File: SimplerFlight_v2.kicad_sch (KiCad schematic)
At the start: 30 parts, among them J1 USB_B_Micro, J2 Conn_01x04_Pin, J3 Conn_01x04_Pin, J4 Conn_01x04_Pin, J5 Conn_01x04_Pin, J6 675031020, SW1 SW_SPDT, U1 AMS1117-3.3, U2 STM32F401RETx, Y1 16MHz

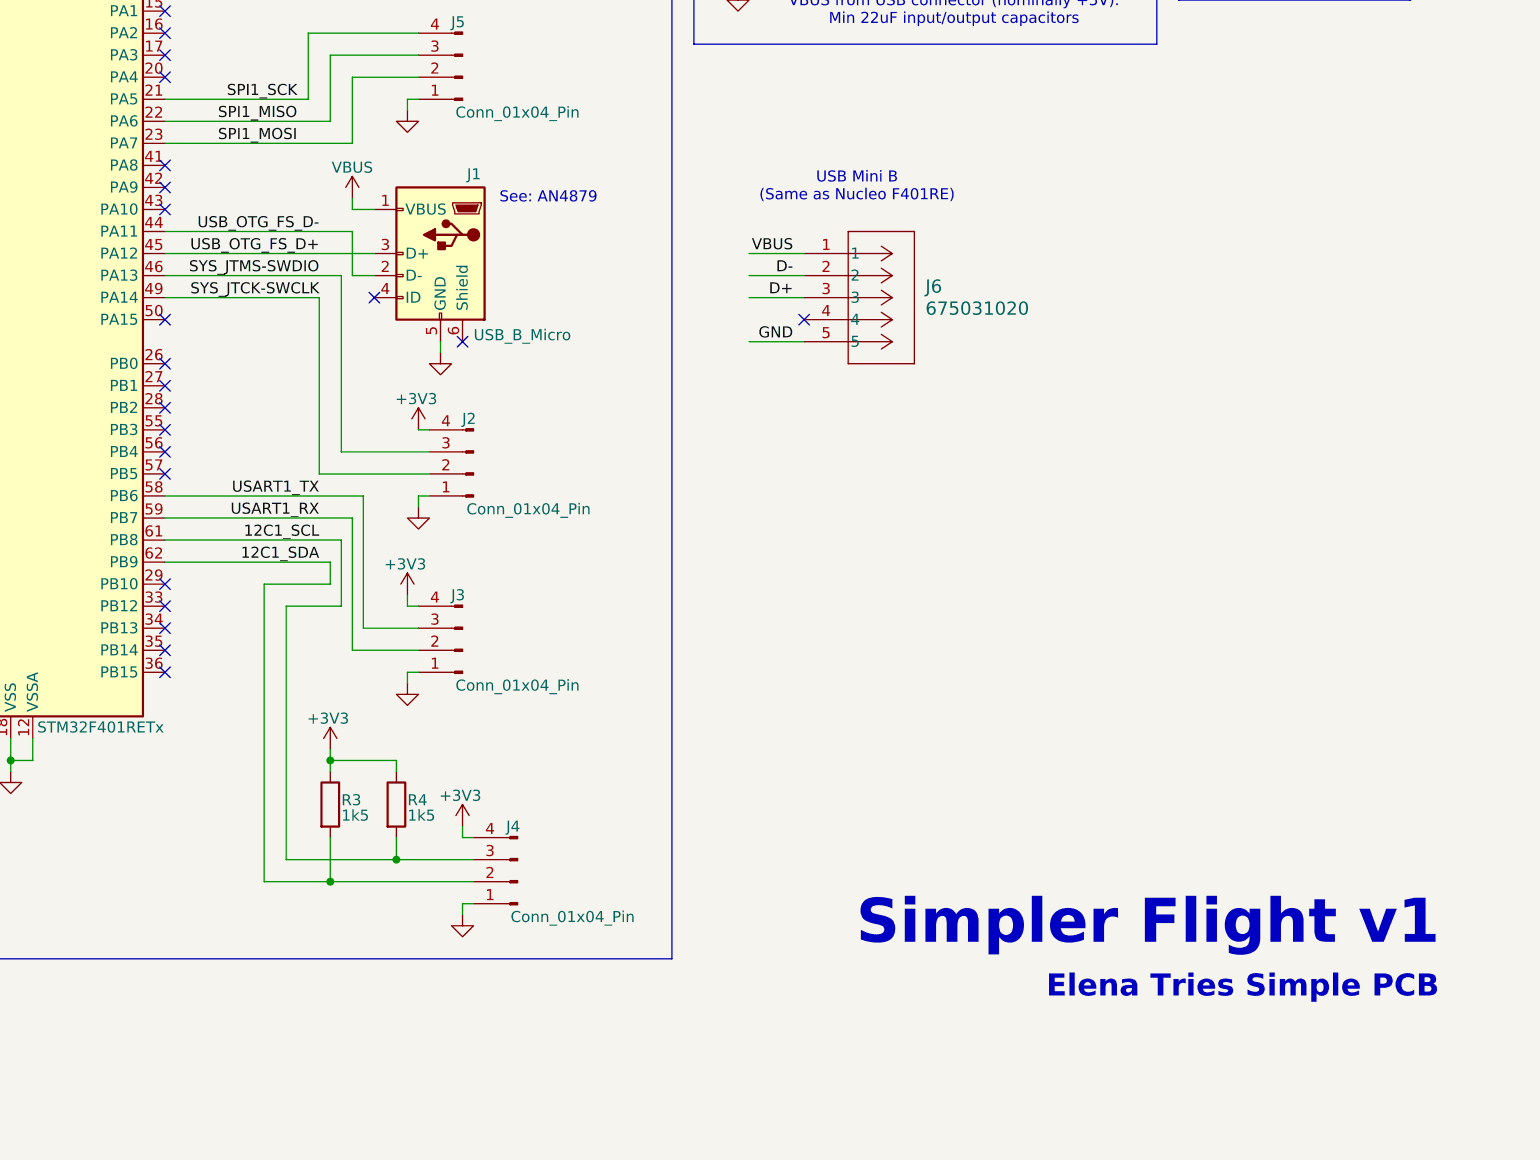
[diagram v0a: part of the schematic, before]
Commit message: Update readme and some silskreen labeles
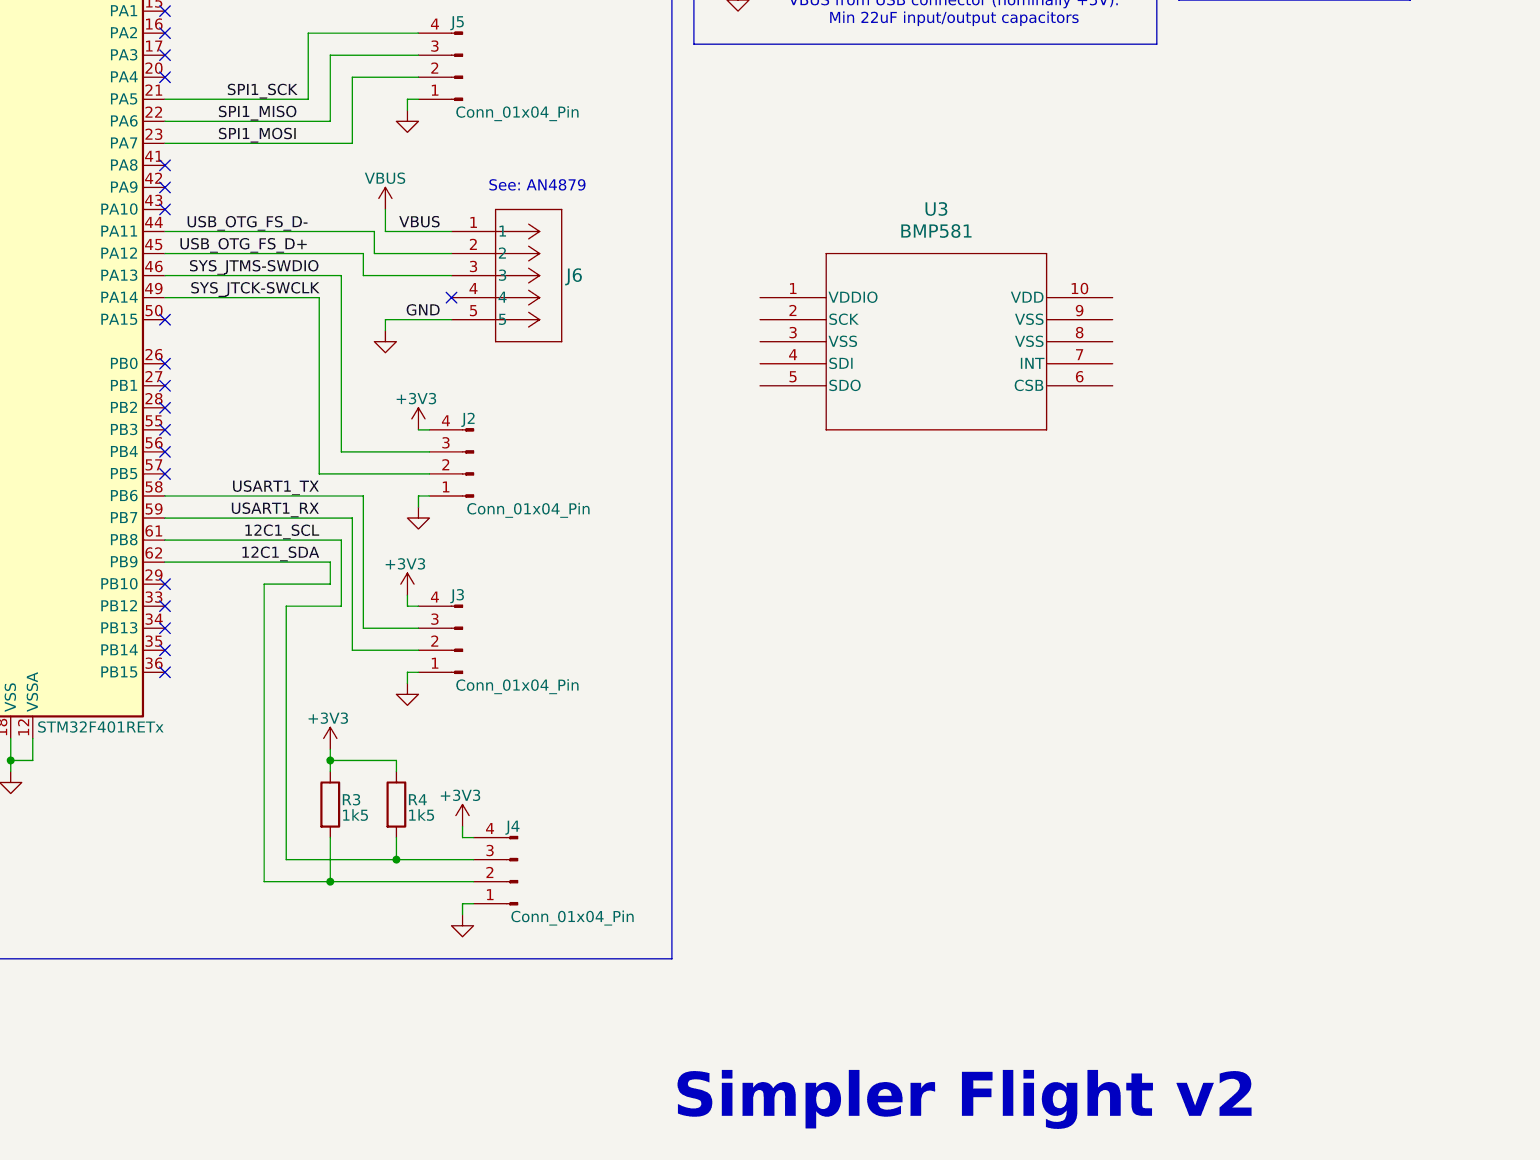
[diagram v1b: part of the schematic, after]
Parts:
- removed J1: USB_B_Micro, Connector_USB:USB_Micro-B_Wuerth_629105150521, symbol Connector:USB_B_Micro
- added U3: BMP581, QFN10_BMP581_BOS, symbol BMP581:BMP581
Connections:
- net D+ is gone; now on net USB_OTG_FS_D+: J6.3
- net D- is gone; now on net USB_OTG_FS_D-: J6.2
- no-connect marks 42 -> 40
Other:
- note added: "Simpler Flight v2"
- note removed: "Elena Tries Simple PCB"
- note removed: "Simpler Flight v1"
- note removed: "USB Mini B (Same as Nucleo F401RE)"
- title: Simpler Flight PCB -> Simpl Flight v2
- moved on the sheet: J6

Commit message: Fix name
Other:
- title: Simpl Flight v2 -> Simpler Flight v2
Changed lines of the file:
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@@
 	(paper "A4")
 	(title_block
-		(title "Simpl Flight v2")
+		(title "Simpler Flight v2")
 		(date "2025-04-20")
 		(rev "1")

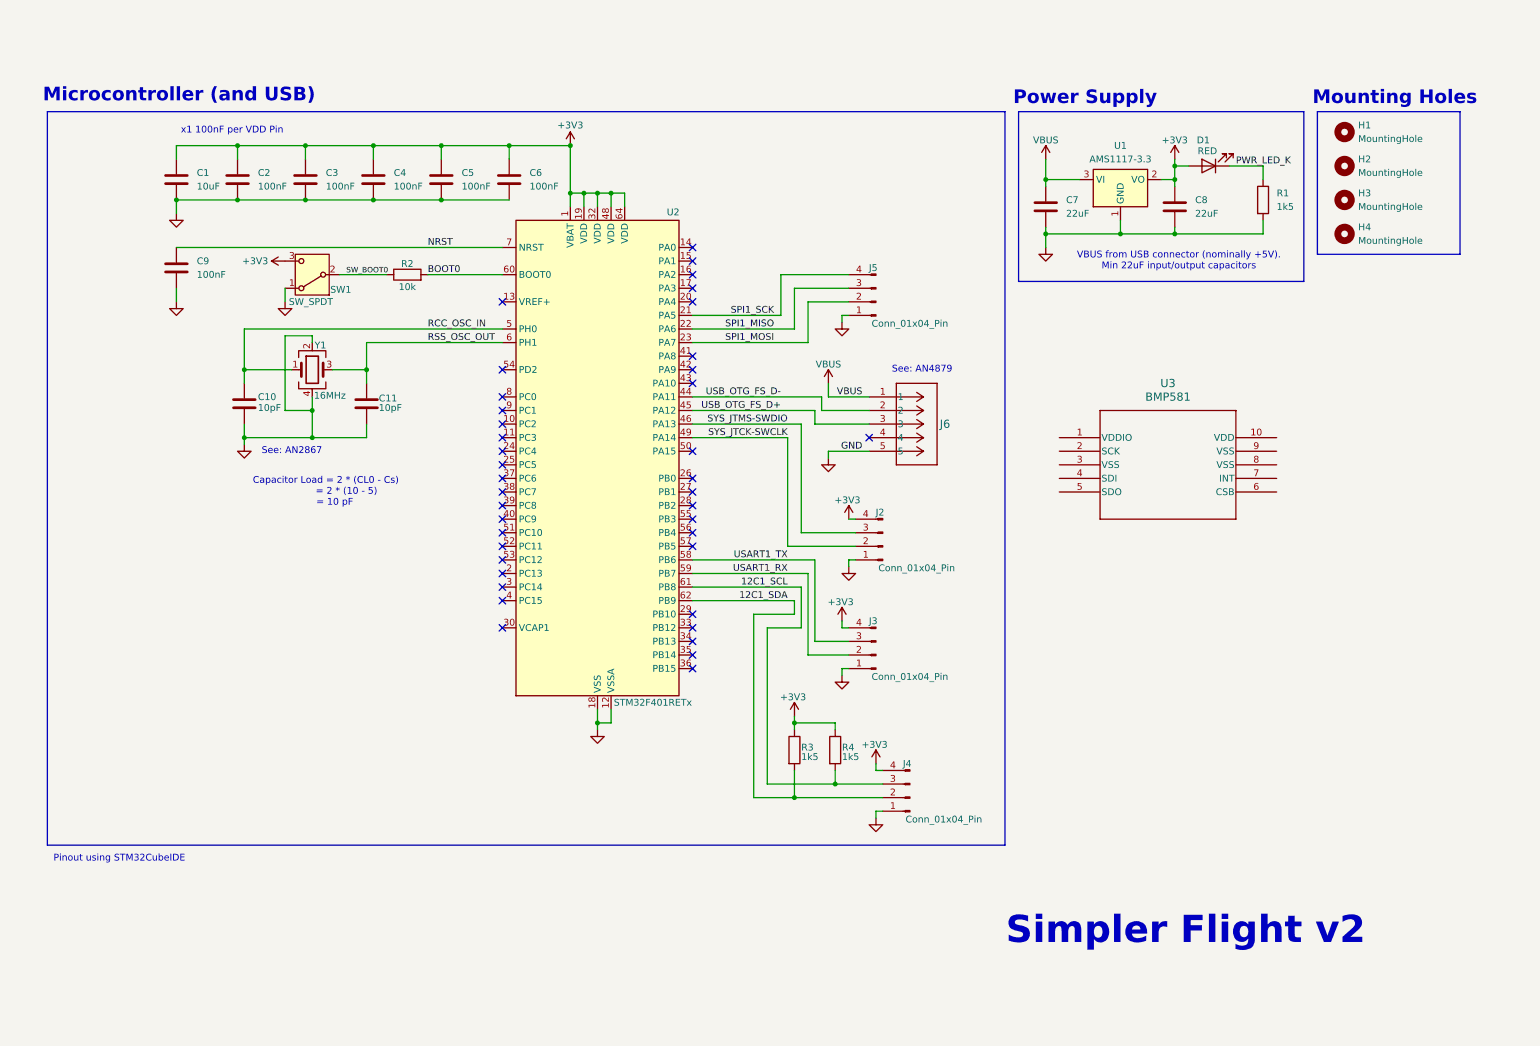
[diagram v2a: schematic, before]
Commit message: Reorganisation and draft of power supply
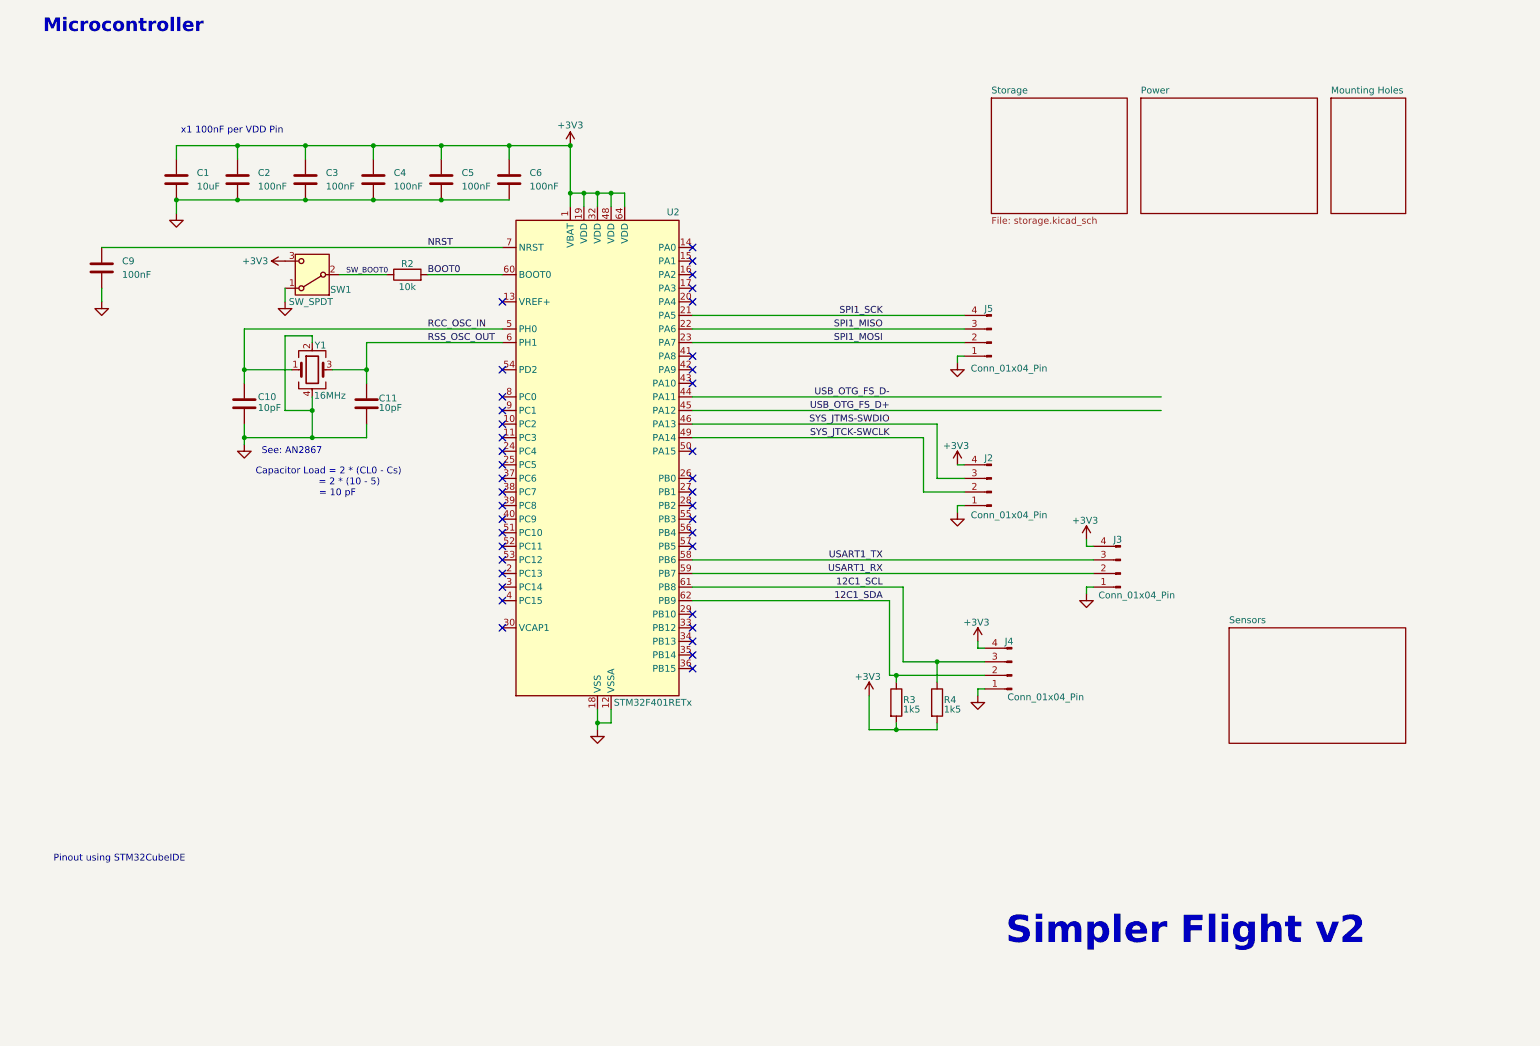
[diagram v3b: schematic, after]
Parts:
- removed C7, C8: 22uF, Capacitor_SMD:C_0805_2012Metric, symbol Device:C
- removed D1: RED, LED_SMD:LED_0805_2012Metric, symbol Device:LED
- removed H1, H2, H3, H4: MountingHole, MountingHole:MountingHole_2.2mm_M2, symbol Mechanical:MountingHole
- removed J6: 675031020, KiCADv6:CON00317_5_MOL, symbol 2025-06-16_04-10-11:675031020
- removed R1: 1k5, Capacitor_SMD:C_0805_2012Metric, symbol Device:R
- removed U1: AMS1117-3.3, Package_TO_SOT_SMD:SOT-223-3_TabPin2, symbol Regulator_Linear:AMS1117-3.3
- removed U3: BMP581, QFN10_BMP581_BOS, symbol BMP581:BMP581
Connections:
- net +3V3: now also R3.2, R4.2; no longer R3.1, R4.1
- net 12C1_SCL: now also R4.1; no longer R4.2
- net 12C1_SDA: now also R3.1; no longer R3.2
- no-connect marks 40 -> 39
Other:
- added sheet Mounting Holes (mounting_holes.kicad_sch)
- added sheet Power (power.kicad_sch)
- added sheet Sensors (sensors.kicad_sch)
- added sheet Storage (storage.kicad_sch)
- note added: "Microcontroller"
- note removed: "Microcontroller (and USB)"
- note removed: "Mounting Holes"
- note removed: "Power Supply"
- note removed: "See: AN4879"
- note removed: "VBUS from USB connector (nominally +5V). Min 22uF input/output capacitors"
- moved on the sheet: C9, J2, J3, J4, J5, R3, R4

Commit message: Update readme
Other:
- note removed: "Microcontroller"
- note removed: "Pinout using STM32CubeIDE"
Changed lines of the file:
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@@
 	(title_block
 		(title "Simpler Flight v2")
-		(date "2025-04-20")
+		(date "2025-06-23")
 		(rev "1")
 		(company "Lulu Systems")
@@
 		)
 	)
-	(text "Pinout using STM32CubeIDE\n"
-		(exclude_from_sim no)
-		(at 28.702 160.02 0)
-		(effects
-			(font
-				(size 1.27 1.27)
-			)
-		)
-	)
 	(text "Capacitor Load = 2 * (CL0 - Cs)\n              = 2 * (10 - 5)\n      = 10 pF\n"
 		(exclude_from_sim no)
@@
 		)
 	)
-	(text "Microcontroller"
-		(exclude_from_sim no)
-		(at 29.464 4.318 0)
-		(effects
-			(font
-				(size 2.54 2.54)
-				(thickness 0.508)
-				(bold yes)
-			)
-		)
-	)
 	(junction
 		(at 118.11 35.56)
@@
 	)
 	(sheet
-		(at 191.77 17.78)
-		(size 25.4 21.59)
+		(at 237.49 67.31)
+		(size 33.02 21.59)
 		(exclude_from_sim no)
 		(in_bom yes)
@@
 		)
 		(property "Sheetname" "Storage"
-			(at 191.77 17.0684 0)
+			(at 237.49 66.5984 0)
 			(effects
 				(font
@@
 		)
 		(property "Sheetfile" "storage.kicad_sch"
-			(at 191.77 39.9546 0)
+			(at 237.49 89.4846 0)
 			(effects
 				(font
@@
 				)
 				(justify left top)
+				(hide yes)
 			)
 		)
@@
 	)
 	(sheet
-		(at 255.27 17.78)
-		(size 13.97 21.59)
+		(at 144.78 171.45)
+		(size 25.4 21.59)
 		(exclude_from_sim no)
 		(in_bom yes)
@@
 		)
 		(property "Sheetname" "Mounting Holes"
-			(at 255.27 17.0684 0)
+			(at 144.78 170.7384 0)
 			(show_name yes)
 			(effects
@@
 		)
 		(property "Sheetfile" "mounting_holes.kicad_sch"
-			(at 255.27 39.9546 0)
+			(at 144.78 193.6246 0)
 			(show_name yes)
 			(effects
@@
 	)
 	(sheet
-		(at 236.22 116.84)
+		(at 237.49 95.25)
 		(size 33.02 21.59)
 		(exclude_from_sim no)
@@
 		)
 		(property "Sheetname" "Sensors"
-			(at 236.22 116.1284 0)
+			(at 237.49 94.5384 0)
 			(effects
 				(font
@@
 		)
 		(property "Sheetfile" "sensors.kicad_sch"
-			(at 236.22 139.0146 0)
+			(at 237.49 117.4246 0)
 			(effects
 				(font
@@
 	)
 	(sheet
-		(at 219.71 17.78)
+		(at 237.49 39.37)
 		(size 33.02 21.59)
 		(exclude_from_sim no)
@@
 		)
 		(property "Sheetname" "Power"
-			(at 219.71 17.0684 0)
+			(at 237.49 38.6584 0)
 			(show_name yes)
 			(effects
@@
 		)
 		(property "Sheetfile" "power.kicad_sch"
-			(at 219.71 39.9546 0)
+			(at 237.49 61.5446 0)
 			(show_name yes)
 			(effects

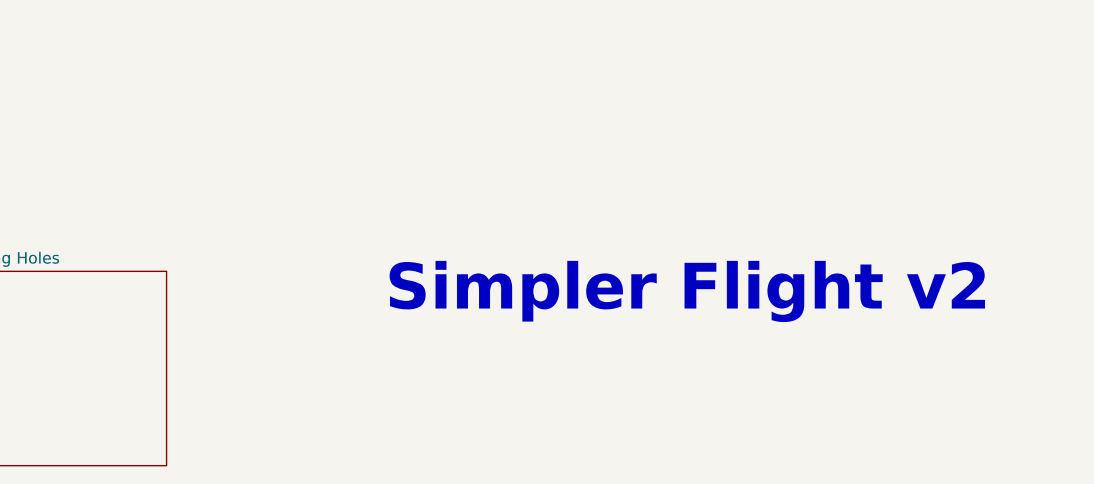
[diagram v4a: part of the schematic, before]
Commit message: Remove redundant diode for camera supply
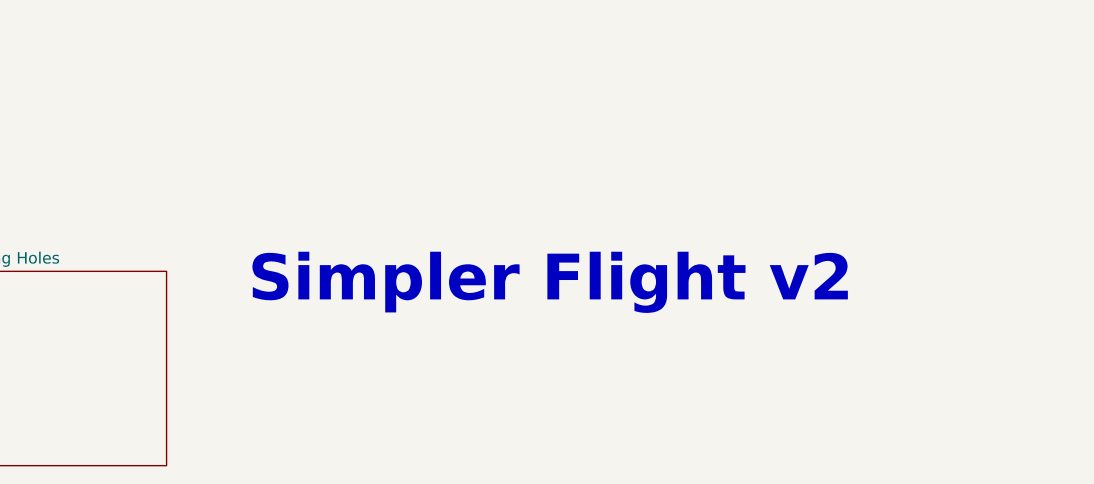
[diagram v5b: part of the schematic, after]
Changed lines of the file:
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@@
 	(text "Simpler Flight v2\n"
 		(exclude_from_sim no)
-		(at 228.092 173.482 0)
+		(at 212.852 172.466 0)
 		(effects
 			(font
@@
 	)
 	(image
-		(at 184.15 172.72)
+		(at 254 172.72)
 		(scale 0.117186)
 		(data "iVBORw0KGgoAAAANSUhEUgAABAAAAAQACAIAAADwf7zUAAAAA3NCSVQICAjb4U/gAAAgAElEQVR4"
